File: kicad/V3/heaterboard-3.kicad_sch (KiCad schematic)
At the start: 26 parts, among them J1 Power In, J2 Heater, J4 Relay, J5 GPIO, J6 GPIO, Q1 Power MOSFET, U1 Voltage Regulator, U2 Current Sensor IC

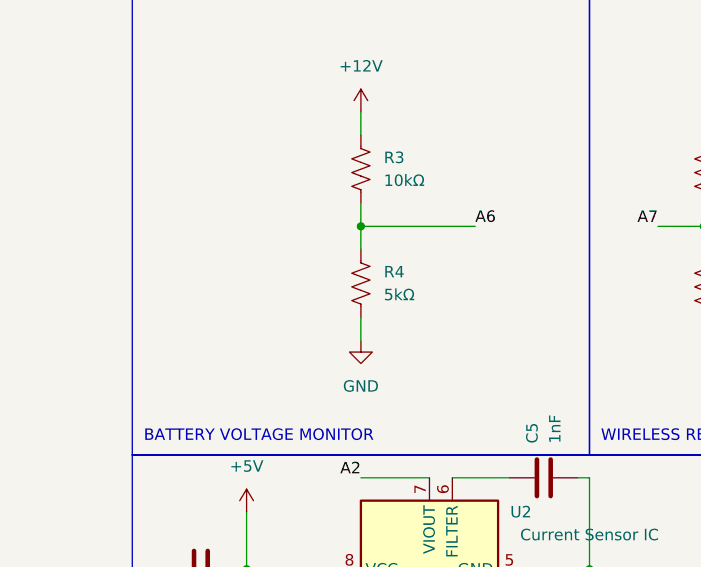
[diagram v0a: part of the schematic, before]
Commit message: voltage divider, code updates
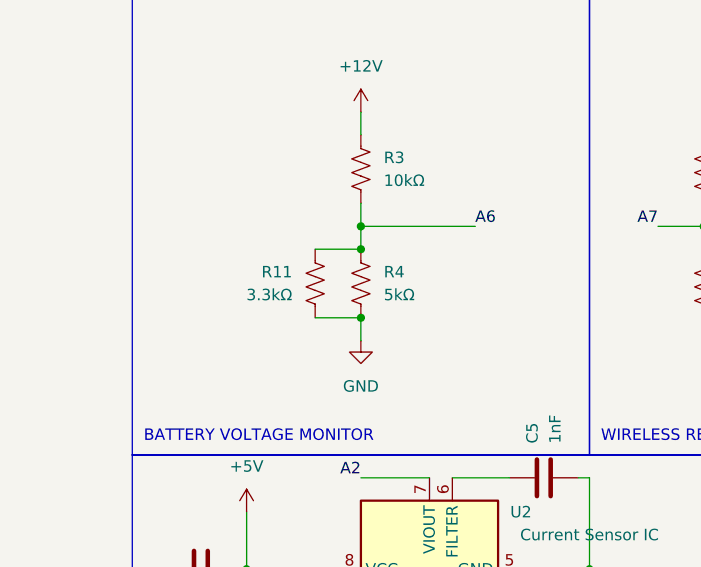
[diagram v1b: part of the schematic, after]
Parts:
- added R11: 3.3kΩ, symbol Device:R_US
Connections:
- net A6: now also R11.1
- net GND: now also R11.2
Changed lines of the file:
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@@
 	)
 	(junction
+		(at 50.8 104.14)
+		(diameter 0)
+		(color 0 0 0 0)
+	)
+	(junction
 		(at 38.1 139.7)
 		(diameter 0)
@@
 	)
 	(junction
+		(at 50.8 111.76)
+		(diameter 0)
+		(color 0 0 0 0)
+	)
+	(junction
 		(at 76.2 165.1)
 		(diameter 0)
@@
 	(wire
 		(pts
+			(xy 45.72 104.14) (xy 50.8 104.14)
+		)
+		(stroke
+			(width 0)
+			(type default)
+		)
+	)
+	(wire
+		(pts
 			(xy 114.3 152.4) (xy 38.1 152.4)
 		)
@@
 	(wire
 		(pts
+			(xy 45.72 111.76) (xy 50.8 111.76)
+		)
+		(stroke
+			(width 0)
+			(type default)
+		)
+	)
+	(wire
+		(pts
 			(xy 38.1 149.86) (xy 53.34 149.86)
 		)
@@
 					(unit 1)
 				)
+			)
+		)
+	)
+	(symbol
+		(lib_id "Device:R_US")
+		(at 45.72 107.95 0)
+		(unit 1)
+		(exclude_from_sim no)
+		(in_bom yes)
+		(on_board yes)
+		(dnp no)
+		(property "Reference" "R11"
+			(at 43.18 106.6799 0)
+			(effects
+				(font
+					(size 1.27 1.27)
+				)
+				(justify right)
+			)
+		)
+		(property "Value" "3.3kΩ"
+			(at 43.18 109.2199 0)
+			(effects
+				(font
+					(size 1.27 1.27)
+				)
+				(justify right)
+			)
+		)
+		(property "Footprint" ""
+			(at 46.736 108.204 90)
+			(effects
+				(font
+					(size 1.27 1.27)
+				)
+				(hide yes)
+			)
+		)
+		(property "Datasheet" "~"
+			(at 45.72 107.95 0)
+			(effects
+				(font
+					(size 1.27 1.27)
+				)
+				(hide yes)
+			)
+		)
+		(property "Description" "Resistor, US symbol"
+			(at 45.72 107.95 0)
+			(effects
+				(font
+					(size 1.27 1.27)
+				)
+				(hide yes)
+			)
+		)
+		(pin "1"
+		)
+		(pin "2"
+		)
+		(instances
+			(project "heaterboard-3"
+				(path "/63b0bf45-0e24-4f26-a68d-dac5d63dd697"
+					(reference "R11")
+					(unit 1)
+				)
